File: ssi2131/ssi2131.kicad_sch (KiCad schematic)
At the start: 2 parts, among them U1 SSI2131, U2 LM4040DBZ-2.5

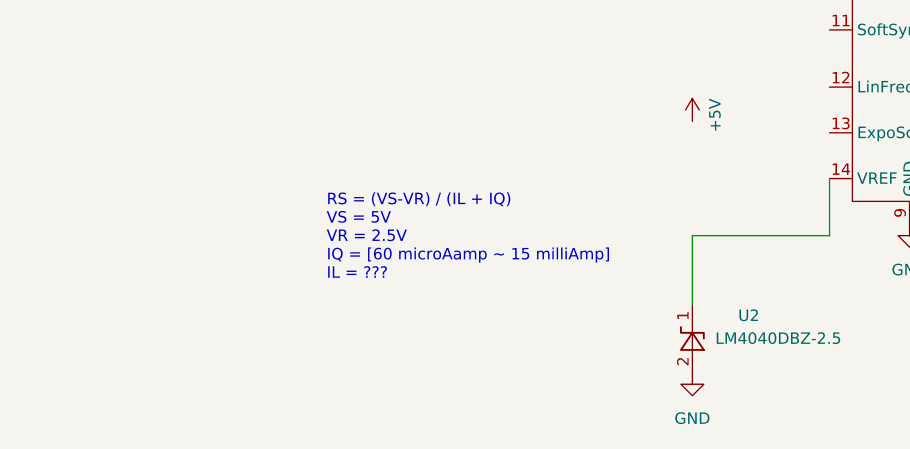
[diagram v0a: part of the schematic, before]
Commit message: add notes on regulator current and resistor
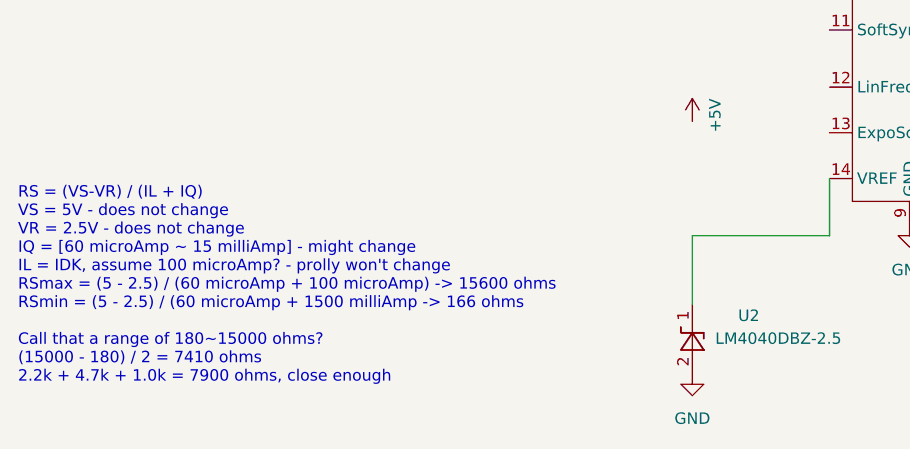
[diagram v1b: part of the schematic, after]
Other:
- note added: "RS = (VS-VR) / (IL + IQ) VS = 5V - does not change VR = 2.5V - does not change IQ = [60 microAmp ~ 15 milliAmp] - might change IL = IDK, assume 100 microAmp? - prolly won't change RSmax = (5 - 2.5) / (60 microAmp + 100 microAmp) -> 15600 ohms RSmin = (5 - 2.5) / (60 microAmp + 1500 milliAmp -> 166 ohms Call that a range of 180~15000 ohms? (15000 - 180) / 2 = 7410 ohms 2.2k + 4.7k + 1.0k = 7900 oh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"
- note removed: "RS = (VS-VR) / (IL + IQ) VS = 5V VR = 2.5V IQ = [60 microAamp ~ 15 milliAmp] IL = ???"
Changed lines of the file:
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@@
     (stroke (width 0) (type default) (color 0 0 0 0))
   )
-  (text "RS = (VS-VR) / (IL + IQ)\nVS = 5V\nVR = 2.5V\nIQ = [60 microAamp ~ 15 milliAmp]\nIL = ???"
-    (at 77.47 133.35 0)
+  (text "RS = (VS-VR) / (IL + IQ)\nVS = 5V - does not change\nVR = 2.5V - does not change\nIQ = [60 microAmp ~ 15 milliAmp] - might change\nIL = IDK, assume 100 microAmp? - prolly won't change\nRSmax = (5 - 2.5) / (60 microAmp + 100 microAmp) -> 15600 ohms\nRSmin = (5 - 2.5) / (60 microAmp + 1500 milliAmp -> 166 ohms\n\nCall that a range of 180~15000 ohms?\n(15000 - 180) / 2 = 7410 ohms\n2.2k + 4.7k + 1.0k = 7900 ohms, close enough"
+    (at 43.18 144.78 0)
     (effects (font (size 1.27 1.27)) (justify left bottom))
   )

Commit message: updates
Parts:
- added C1, C2, C3: 10 nF, Capacitor_THT:C_Disc_D9.0mm_W2.5mm_P5.00mm, symbol Device:C
- added C4, C6: 0.1 uF, Capacitor_THT:C_Disc_D9.0mm_W2.5mm_P5.00mm, symbol Device:C
- added C5: 3.9 nF, Capacitor_THT:C_Disc_D9.0mm_W2.5mm_P5.00mm, symbol Device:C
- added J1: Saw Out, Connector_Audio:Jack_3.5mm_QingPu_WQP-PJ398SM_Vertical_CircularHoles, symbol Connector:AudioJack2
- added J2: Pulse Out, Connector_Audio:Jack_3.5mm_QingPu_WQP-PJ398SM_Vertical_CircularHoles, symbol Connector:AudioJack2
- added J3: Tri Out, Connector_Audio:Jack_3.5mm_QingPu_WQP-PJ398SM_Vertical_CircularHoles, symbol Connector:AudioJack2
- added J4: Hard Sync, Connector_Audio:Jack_3.5mm_QingPu_WQP-PJ398SM_Vertical_CircularHoles, symbol Connector:AudioJack2
- added J5: Soft Sync, Connector_Audio:Jack_3.5mm_QingPu_WQP-PJ398SM_Vertical_CircularHoles, symbol Connector:AudioJack2
- added J6: Expo Freq, Connector_Audio:Jack_3.5mm_QingPu_WQP-PJ398SM_Vertical_CircularHoles, symbol Connector:AudioJack2
- added R1: 4.7 kOhms, Resistor_THT:R_Axial_DIN0207_L6.3mm_D2.5mm_P10.16mm_Horizontal, symbol Device:R_US
- added R2: 2.2 kOhms, Resistor_THT:R_Axial_DIN0207_L6.3mm_D2.5mm_P10.16mm_Horizontal, symbol Device:R_US
- added R3: 1 kOhms, Resistor_THT:R_Axial_DIN0207_L6.3mm_D2.5mm_P10.16mm_Horizontal, symbol Device:R_US
- added R4: 10 kOhms, Resistor_THT:R_Axial_DIN0207_L6.3mm_D2.5mm_P10.16mm_Horizontal, symbol Device:R_US
- added R5: 220 Ohms, Resistor_THT:R_Axial_DIN0207_L6.3mm_D2.5mm_P10.16mm_Horizontal, symbol Device:R_US
- added R6: 4.3 kOhms, Resistor_THT:R_Axial_DIN0207_L6.3mm_D2.5mm_P10.16mm_Horizontal, symbol Device:R_US
- added R7: 499 kOhms, Resistor_THT:R_Axial_DIN0207_L6.3mm_D2.5mm_P10.16mm_Horizontal, symbol Device:R_US
- added R8: 22.1 kOhms, Resistor_THT:R_Axial_DIN0207_L6.3mm_D2.5mm_P10.16mm_Horizontal, symbol Device:R_US
- added R?: 47 kOhms, Resistor_THT:R_Axial_DIN0207_L6.3mm_D2.5mm_P10.16mm_Horizontal, symbol Device:R_US
- added R? (x2): 100 kOhms, Resistor_THT:R_Axial_DIN0207_L6.3mm_D2.5mm_P10.16mm_Horizontal, symbol Device:R_US
- added R?: 220 kOhms, Resistor_THT:R_Axial_DIN0207_L6.3mm_D2.5mm_P10.16mm_Horizontal, symbol Device:R_US
- added R?: 47 Ohms, Resistor_THT:R_Axial_DIN0207_L6.3mm_D2.5mm_P10.16mm_Horizontal, symbol Device:R_US
- added RV1: PWM Knob - 5 kOhms, Potentiometer_THT:Potentiometer_Alpha_RD901F-40-00D_Single_Vertical, symbol Device:R_Potentiometer_US
- added RV2: Expo Scale Knob - 5 kOhms, Potentiometer_THT:Potentiometer_Bourns_3296W_Vertical, symbol Device:R_Potentiometer_US
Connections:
- net +5V: now also C4.2, R1.1
- net -12V: now also C6.2
- net GND: now also C3.1, C4.1, C5.2, C6.1, J1.S, J2.S, J3.S, J4.S, J5.S, J6.S, R4.1, R6.2, RV1.3
- net at U1.1 (Saw): now also J1.T
- net at U1.10 (HardSync): now also C1.2, R4.2
- net at U1.11 (SoftSync): now also C2.1
- net at U1.12 (LinFreq): now also R7.1
- net at U1.13 (ExpoScale): now also RV2.1
- net +2V5: now reaches U1.14 (VREF), U2.1 (K)
- net +2V5: now also R3.2, R7.2, R8.2, RV1.1
- net at U1.15 (BWComp): now also R5.1
- net at U1.2 (Pulse): now also J2.T
- net at U1.3 (PWMCtrl): now also RV1.2
- net at U1.4 (Tri): now also J3.T
- net at U1.5 (HFTrack): now also R6.1, R?.2
- net at U1.6 (ExpoFreq): now also R?.1, R?.2, R?.2
- net at U1.8 (TCAP): now also C5.1
- new net: C3.2, R?.2
- new net: C1.1, J4.T
- new net: R?.1, R?.2
- new net: R8.1, RV2.2, RV2.3
- new net: R2.2, R3.1
- new net: J6.T, R?.1, R?.1
- new net: R5.2, R?.1
- new net: R1.2, R2.1
- new net: C2.2, J5.T
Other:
- note added: "R1 + R2 + R3 = RS"
- note added: "Use precision 10-turn pot, such as Bourns PV36Y"
- moved on the sheet: U1, U2

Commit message: starting on pcb
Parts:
- added C7: 680 pF, Capacitor_THT:C_Disc_D9.0mm_W2.5mm_P5.00mm, symbol Device:C
- added J7: 16-Pin uZeus Power Header, Connector_PinHeader_2.54mm:PinHeader_2x08_P2.54mm_Horizontal, symbol Connector_Generic:Conn_02x08_Odd_Even
- added R10, R9: 1 MOhms, Resistor_THT:R_Axial_DIN0207_L6.3mm_D2.5mm_P10.16mm_Horizontal, symbol Device:R_US
- added R13: 100 Ohms, Resistor_THT:R_Axial_DIN0207_L6.3mm_D2.5mm_P10.16mm_Horizontal, symbol Device:R_US
- C5: value 3.9 nF -> 3.3 nF
- R6: value 4.3 kOhms -> 4.7 kOhms
- R7: value 499 kOhms -> 47 kOhms
- R8: value 22.1 kOhms -> 22 kOhms
- gave numbers to parts that had none: 5
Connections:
- net +2V5: now also R10.1, R9.1; no longer R7.2
- net +5V: now also J7.9 (Pin_9)
- net -12V: now also J7.1 (Pin_1)
- net GND: now also R7.2, C7.2, J7.3 (Pin_3), J7.5 (Pin_5), J7.7 (Pin_7)
- net at R15.2, R6.1, U1.5 (HFTrack): now also R7.1
- net at RV2.2, RV2.3: now also R13.1; no longer R8.1
- net at C5.1, U1.8 (TCAP): now also C7.1
- net at U1.12 (LinFreq): now also R10.2, R9.2; no longer R7.1
- new net: R13.2, R8.1
- no-connect marks 0 -> 11
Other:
- note added: "3.9 nF"
- note added: "4.3 kOhms"
- note added: "49.9 kOhms"
- note added: "499 kOhms"
- moved on the sheet: C1, C2, C3, C4, C5, C6, J1, J2, J3, J4, J5, J6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

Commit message: PCB attempt 1
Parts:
- removed J6: Expo Freq, Connector_Audio:Jack_3.5mm_QingPu_WQP-PJ398SM_Vertical_CircularHoles, symbol Connector:AudioJack2
- added J9: Expo Freq, Connector_Audio:Jack_3.5mm_QingPu_WQP-PJ398SM_Vertical_CircularHoles, symbol Connector:AudioJack2
- C1, C2, C3, C4, C5, C6, C7: footprint Capacitor_THT:C_Disc_D9.0mm_W2.5mm_P5.00mm -> Capacitor_THT:C_Disc_D6.0mm_W2.5mm_P5.00mm
- J7: footprint Connector_PinHeader_2.54mm:PinHeader_2x08_P2.54mm_Horizontal -> Connector_PinHeader_2.54mm:PinHeader_2x08_P2.54mm_Vertical
- R1, R10, R13, R16, R2, R3, R4, R5, R6, R7, R8, R9: footprint Resistor_THT:R_Axial_DIN0207_L6.3mm_D2.5mm_P10.16mm_Horizontal -> Resistor_THT:R_Axial_DIN0207_L6.3mm_D2.5mm_P2.54mm_Vertical
- R11: value 100 kOhms -> 220 kOhms; footprint Resistor_THT:R_Axial_DIN0207_L6.3mm_D2.5mm_P10.16mm_Horizontal -> Resistor_THT:R_Axial_DIN0207_L6.3mm_D2.5mm_P2.54mm_Vertical
- R12: value 100 kOhms -> 47 kOhms; footprint Resistor_THT:R_Axial_DIN0207_L6.3mm_D2.5mm_P10.16mm_Horizontal -> Resistor_THT:R_Axial_DIN0207_L6.3mm_D2.5mm_P2.54mm_Vertical
- R14: value 220 kOhms -> 100 kOhms; footprint Resistor_THT:R_Axial_DIN0207_L6.3mm_D2.5mm_P10.16mm_Horizontal -> Resistor_THT:R_Axial_DIN0207_L6.3mm_D2.5mm_P2.54mm_Vertical
- R15: value 47 kOhms -> 100 kOhms; footprint Resistor_THT:R_Axial_DIN0207_L6.3mm_D2.5mm_P10.16mm_Horizontal -> Resistor_THT:R_Axial_DIN0207_L6.3mm_D2.5mm_P2.54mm_Vertical
- RV2: value Expo Scale Knob - 5 kOhms -> Expo Scale Trim - 5 kOhms
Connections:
- net +5V: now also J7.11 (Pin_11), J7.12 (Pin_12); no longer J7.9 (Pin_9)
- net -12V: now also J7.2 (Pin_2)
- net GND: now also J7.4 (Pin_4), J7.6 (Pin_6), J7.8 (Pin_8), J9.S
- net HardSync: now reaches C1.2, R4.2, U1.10 (HardSync)
- net at R15.1: now also R14.1, J9.T; no longer R14.2
- net HFTrack: now reaches R6.1, R7.1, U1.5 (HFTrack)
- net HFTrack: now also R12.1; no longer R15.2
- net SawOut: now reaches J1.T, U1.1 (Saw)
- net at R11.1: now also R12.2; no longer R12.1
- net ExpoFreq: now reaches R11.2, U1.6 (ExpoFreq)
- net ExpoFreq: now also R14.2, R15.2; no longer R12.2, R14.1
- net TCAP: now reaches C5.1, C7.1, U1.8 (TCAP)
- net BWComp: now reaches R5.1, U1.15 (BWComp)
- net LinFreq: now reaches R10.2, R9.2, U1.12 (LinFreq)
- net SoftSync: now reaches C2.1, U1.11 (SoftSync)
- net ExpoScale: now reaches RV2.1, U1.13 (ExpoScale)
- net PulseOut: now reaches J2.T, U1.2 (Pulse)
- net PWMCtrl: now reaches RV1.2, U1.3 (PWMCtrl)
- net TriOut: now reaches J3.T, U1.4 (Tri)
- no-connect marks 11 -> 6
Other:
- note added: "CORE"
- note added: "EXPO CONVERTER FREQ COMPENSATION"
- note added: "OSC OUT"
- note added: "POWER"
- note added: "RS = (VS-VR) / (IL + IQ) VS = 5V - does not change VR = 2.5V - does not change IQ = [60 uAmp ~ 15 mAmp] - might change IL = IDK, assume 100 uAmp? - prolly won't change RSmax = (5 - 2.5) / (60 uAmp + 100 uAmp) -> 15600 ohms RSmin = (5 - 2.5) / (60 uAmp + 1500 mAmp -> 166 ohms Call that a range of 180~15000 ohms? (15000 - 180) / 2 = 7410 ohms 2.2k + 4.7k + 1.0k = 7900 ohms, close enough"
- note added: "SYNCS"
- note added: "TUNING"
- note added: "V/OCT"
- note removed: "RS = (VS-VR) / (IL + IQ) VS = 5V - does not change VR = 2.5V - does not change IQ = [60 microAmp ~ 15 milliAmp] - might change IL = IDK, assume 100 microAmp? - prolly won't change RSmax = (5 - 2.5) / (60 microAmp + 100 microAmp) -> 15600 ohms RSmin = (5 - 2.5) / (60 microAmp + 1500 milliAmp -> 166 ohms Call that a range of 180~15000 ohms? (15000 - 180) / 2 = 7410 ohms 2.2k + 4.7k + 1.0k = 7900 oh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"
- moved on the sheet: C1, C2, C5, C6, C7, J1, J2, J3, J4, J5, J7, R10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

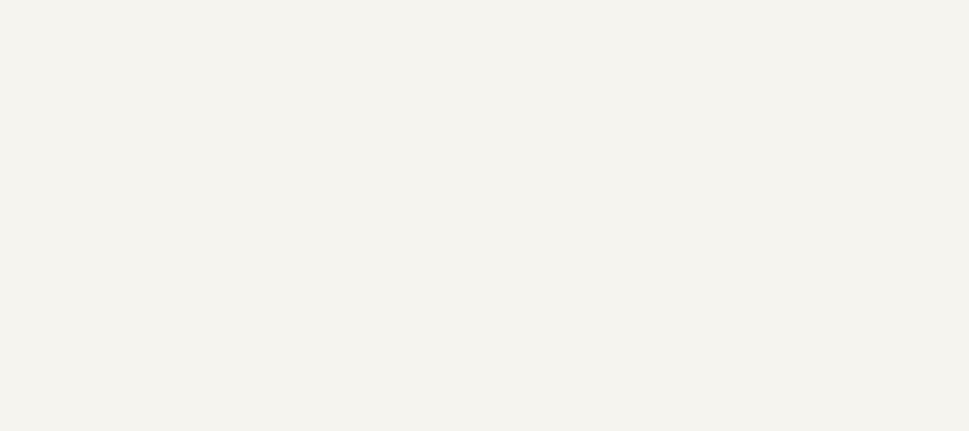
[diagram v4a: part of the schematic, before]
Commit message: Add revision info, adjust tracks and spacing
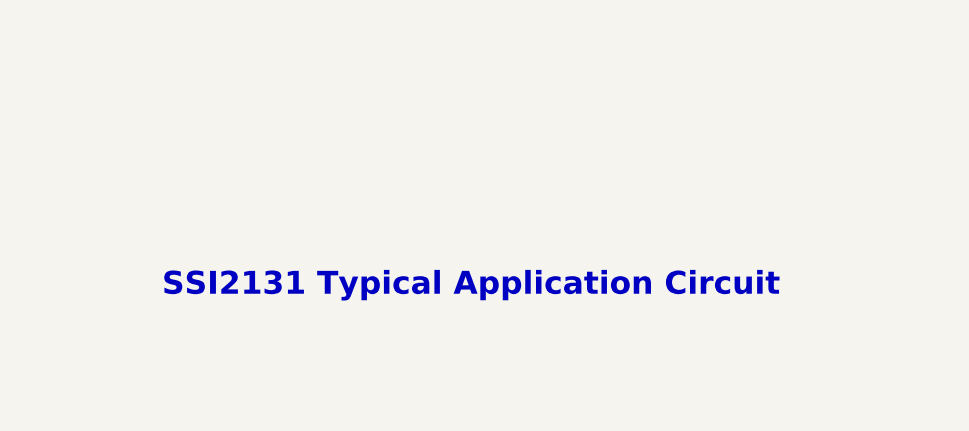
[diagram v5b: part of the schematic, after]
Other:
- note added: "SSI2131 Typical Application Circuit"
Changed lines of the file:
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@@
     (stroke (width 0) (type default) (color 0 0 0 0))
+  )
+  (text "SSI2131 Typical Application Circuit" (at 194.31 175.26 0)
+    (effects (font (size 2.54 2.54) (thickness 0.508) bold) (justify left bottom))
   )
   (text "49.9\nkOhms" (at 134.62 38.1 0)

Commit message: rework PCB layout
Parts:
- removed C7: 680 pF, Capacitor_THT:C_Disc_D6.0mm_W2.5mm_P5.00mm, symbol Device:C
- removed R10: 1 MOhms, Resistor_THT:R_Axial_DIN0207_L6.3mm_D2.5mm_P2.54mm_Vertical, symbol Device:R_US
- removed R12, R7: 47 kOhms, Resistor_THT:R_Axial_DIN0207_L6.3mm_D2.5mm_P2.54mm_Vertical, symbol Device:R_US
- removed R13: 100 Ohms, Resistor_THT:R_Axial_DIN0207_L6.3mm_D2.5mm_P2.54mm_Vertical, symbol Device:R_US
- removed R15: 100 kOhms, Resistor_THT:R_Axial_DIN0207_L6.3mm_D2.5mm_P2.54mm_Vertical, symbol Device:R_US
- removed R16: 47 Ohms, Resistor_THT:R_Axial_DIN0207_L6.3mm_D2.5mm_P2.54mm_Vertical, symbol Device:R_US
- removed R2: 2.2 kOhms, Resistor_THT:R_Axial_DIN0207_L6.3mm_D2.5mm_P2.54mm_Vertical, symbol Device:R_US
- removed R3: 1 kOhms, Resistor_THT:R_Axial_DIN0207_L6.3mm_D2.5mm_P2.54mm_Vertical, symbol Device:R_US
- C5: value 3.3 nF -> 3.9 nF
- R1: value 4.7 kOhms -> 7.5 kOhms
- R11: value 220 kOhms -> 267 kOhms
- R14: value 100 kOhms -> 49.9 kOhms
- R5: value 220 Ohms -> 267 Ohms
- R6: value 4.7 kOhms -> 4.3 kOhms
- R8: value 22 kOhms -> 22.1 kOhms
- R9: value 1 MOhms -> 499 kOhms
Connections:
- net +2V5: now also R1.2
- net HFTrack: now also R11.1
- net at R5.2: now also C3.2
- net at R8.1: now also RV2.2, RV2.3
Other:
- note added: "RS = (VS-VR) / (IL + IQ) VS = 5V - does not change VR = 2.5V - does not change IQ = [60 uAmp ~ 15 mAmp] - might change IL = IDK, assume 100 uAmp? - prolly won't change RSmax = (5 - 2.5) / (60 uAmp + 100 uAmp) -> 15600 ohms RSmin = (5 - 2.5) / (60 uAmp + 1500 mAmp -> 166 ohms Call that a range of 180~15000 ohms? (15000 - 180) / 2 = 7410 ohms 7500 ohms @ 1% tolerance is close enough"
- note removed: "3.9 nF"
- note removed: "4.3 kOhms"
- note removed: "49.9 kOhms"
- note removed: "499 kOhms"
- note removed: "R1 + R2 + R3 = RS"
- note removed: "RS = (VS-VR) / (IL + IQ) VS = 5V - does not change VR = 2.5V - does not change IQ = [60 uAmp ~ 15 mAmp] - might change IL = IDK, assume 100 uAmp? - prolly won't change RSmax = (5 - 2.5) / (60 uAmp + 100 uAmp) -> 15600 ohms RSmin = (5 - 2.5) / (60 uAmp + 1500 mAmp -> 166 ohms Call that a range of 180~15000 ohms? (15000 - 180) / 2 = 7410 ohms 2.2k + 4.7k + 1.0k = 7900 ohms, close enough"
- moved on the sheet: C1, C2, C5, J1, J2, J3, J4, J5, J9, R11, R14, R4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
